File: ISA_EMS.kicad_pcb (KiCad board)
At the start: 2 copper layers, 176.5 x 102.9 mm, 57 parts, among them J1 ISA BUS, J2 EMS Address, J3 ROM Config, U1 74HCT688, U10 74HCT32, U11 74HCT04, U12 74ACT245, U13 AS6C4008-55PCN, U14 AS6C4008-55PCN, U15 AS6C4008-55PCN, U16 AS6C4008-55PCN, U17 74HCT138, U18 74LS573, U19 74LS573, U2 SST39SF040, U20 74LS573, U21 74LS573, U3 AS6C4008-55PCN, U4 AS6C4008-55PCN, U5 AS6C4008-55PCN, U6 AS6C4008-55PCN, U7 74HCT688, U8 74HCT688, U9 74HCT139

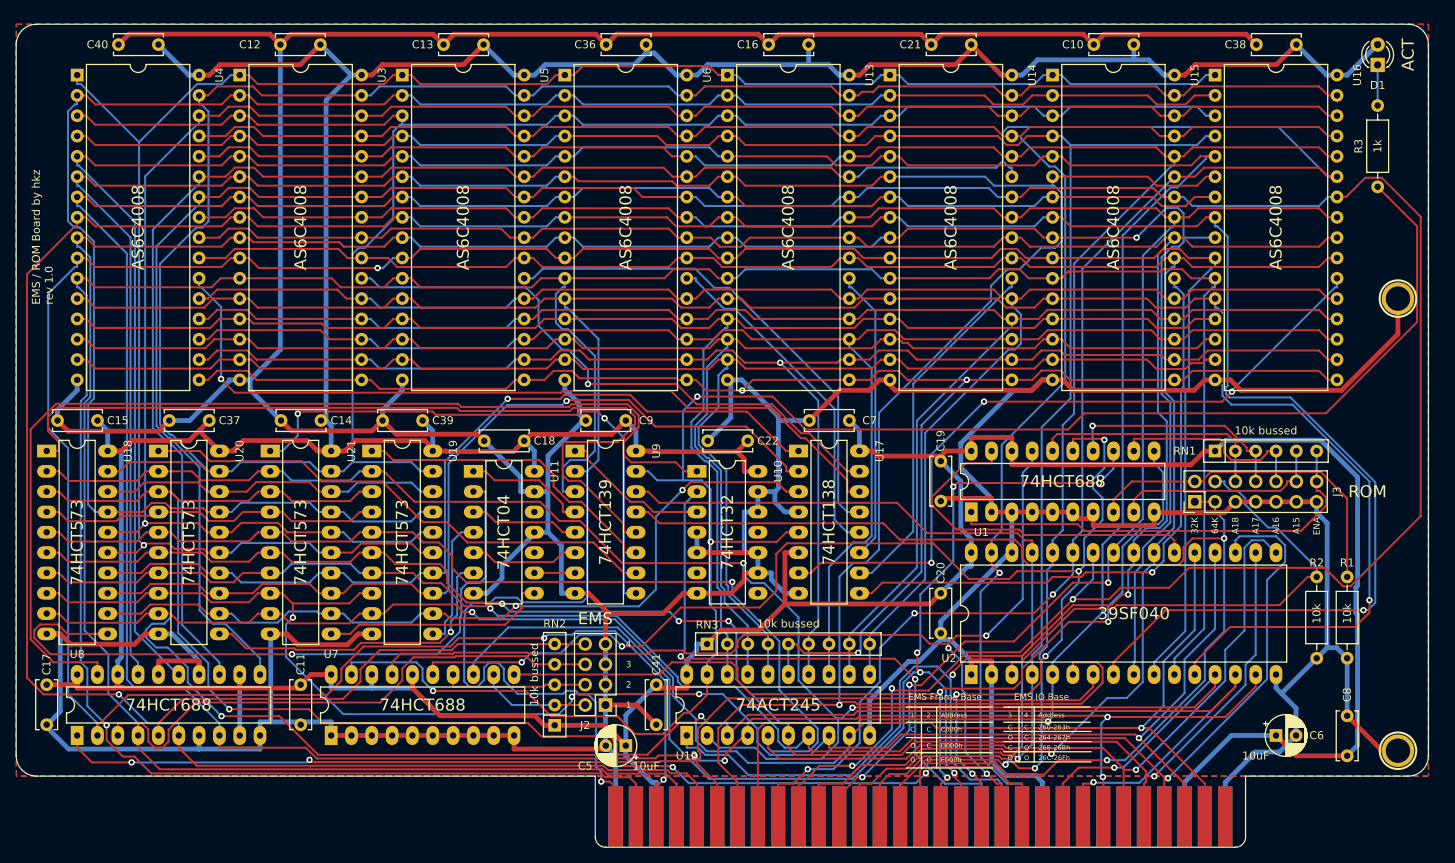
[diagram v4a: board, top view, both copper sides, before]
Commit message: Reorganize board a bit
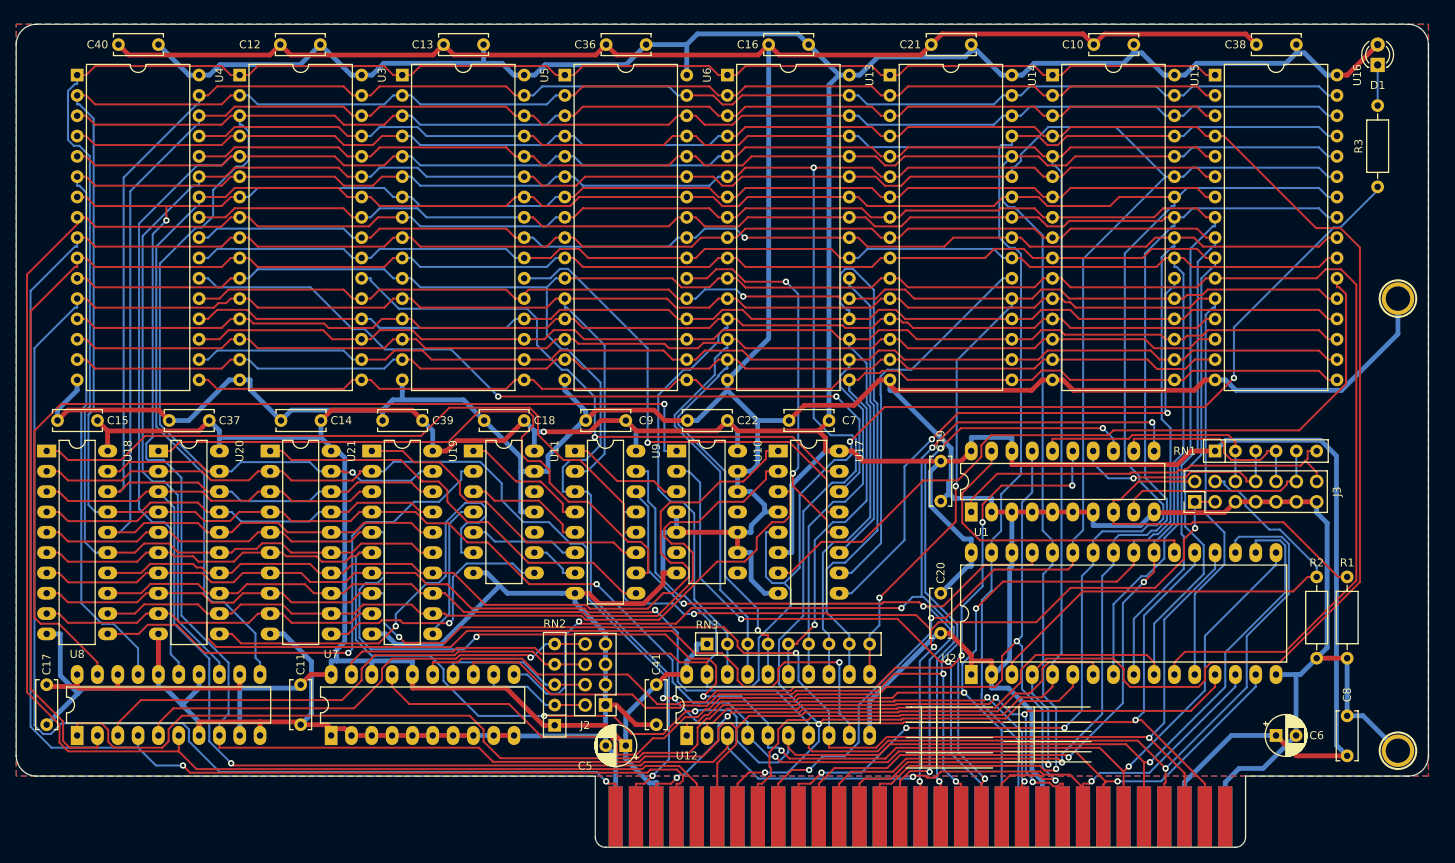
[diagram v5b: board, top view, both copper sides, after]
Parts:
- moved U10 3.59 mm to (221.0, 153.7)
- moved C22 3.59 mm to (227.3, 149.9)
- moved U11 2.54 mm to (195.6, 153.7)
- moved C18 2.54 mm to (201.9, 149.9)
- moved C7 2.54 mm to (240.0, 149.9)
- moved U17 2.54 mm to (233.7, 153.7)
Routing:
- net /A12: track 254.1 -> 306.1 mm
- net /A1: track 367.2 -> 315.3 mm
- net /D2: track 229.2 -> 182.6 mm, vias 5 -> 3
- net /A9: track 375.9 -> 337.3 mm
- net /A4: track 402.8 -> 370.6 mm, vias 2 -> 0
- net /A18: track 162.4 -> 131.2 mm, vias 7 -> 4
- net /A15: track 153.0 -> 122.2 mm, vias 2 -> 4
- net /A0: track 334.6 -> 362.7 mm, vias 2 -> 1
- net /D0: track 220.8 -> 195.4 mm, vias 3 -> 5
- net /D7: track 194.3 -> 218.9 mm
- net GND: track 908.6 -> 884.8 mm
- net /A8: track 357.7 -> 334.0 mm, vias 3 -> 2
- net /~REG0-OE: track 108.7 -> 86.7 mm
- net /REG0-LOAD: track 87.4 -> 65.9 mm
- net /D4: track 199.3 -> 219.2 mm, vias 4 -> 3
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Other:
- board text removed: "1"
- board text removed: "10k"
- board text removed: "10k bussed"
- board text removed: "10uF"
- board text removed: "1k"
- board text removed: "2"
- board text removed: "260-263h"
- board text removed: "264-267h"
- board text removed: "268-26Bh"
- board text removed: "26C-26Fh"
- board text removed: "3"
- board text removed: "32K"
- board text removed: "39SF040"
- board text removed: "4"
- board text removed: "64K"
- board text removed: "74ACT245"
- board text removed: "74HCT04"
- board text removed: "74HCT138"
- board text removed: "74HCT139"
- board text removed: "74HCT32"
- board text removed: "74HCT573"
- board text removed: "74HCT688"
- board text removed: "A15"
- board text removed: "A16"
- board text removed: "A17"
- board text removed: "A18"
- board text removed: "ACT"
- board text removed: "AS6C4008"
- board text removed: "Address"
- board text removed: "C"
- board text removed: "C000h"
- board text removed: "D000h"
- board text removed: "E000h"
- board text removed: "EMS"
- board text removed: "EMS / ROM Board by hkz rev 1.0"
- board text removed: "EMS Frame Base"
- board text removed: "EMS IO Base"
- board text removed: "ENA"
- board text removed: "O"
- board text removed: "ROM"

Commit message: Redoing silkscreen
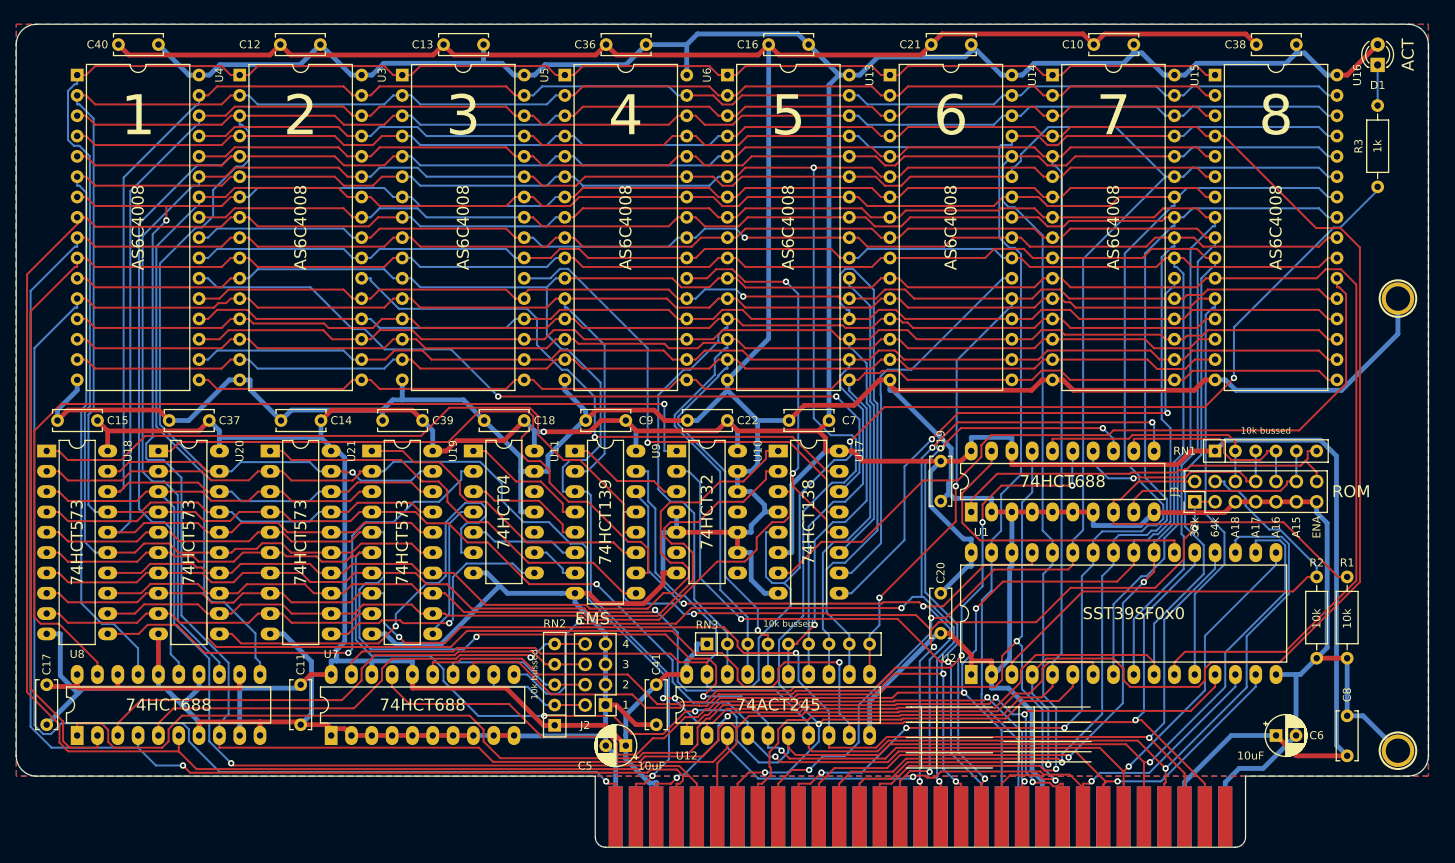
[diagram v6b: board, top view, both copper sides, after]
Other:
- board text added: "1"
- board text added: "10k"
- board text added: "10k bussed"
- board text added: "10uF"
- board text added: "1k"
- board text added: "2"
- board text added: "3"
- board text added: "32k"
- board text added: "4"
- board text added: "5"
- board text added: "6"
- board text added: "64k"
- board text added: "7"
- board text added: "74ACT245"
- board text added: "74HCT04"
- board text added: "74HCT138"
- board text added: "74HCT139"
- board text added: "74HCT32"
- board text added: "74HCT573"
- board text added: "74HCT688"
- board text added: "8"
- board text added: "A15"
- board text added: "A16"
- board text added: "A17"
- board text added: "A18"
- board text added: "ACT"
- board text added: "AS6C4008"
- board text added: "EMS"
- board text added: "ENA"
- board text added: "ROM"
- board text added: "SST39SF0x0"
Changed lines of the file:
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@@
   (general
     (thickness 1.6)
-    (drawings 41)
+    (drawings 92)
     (tracks 3500)
     (zones 0)
@@
   (page A3)
   (layers
-    (0 F.Cu signal)
-    (31 B.Cu signal)
+    (0 F.Cu signal hide)
+    (31 B.Cu signal hide)
     (32 B.Adhes user)
     (33 F.Adhes user)
@@
     (descr "Through hole straight pin header, 2x07, 2.54mm pitch, double rows")
     (tags "Through hole pin header THT 2x07 2.54mm double row")
-    (fp_text reference J3 (at 1.27 17.78 90) (layer F.SilkS)
+    (fp_text reference J3 (at 1.27 -2.54 90) (layer F.SilkS)
       (effects (font (size 1 1) (thickness 0.15)))
     )
@@
     )
   )
+  (gr_text A15 (at 298.45 163.195 90) (layer F.SilkS)
+    (effects (font (size 1 1) (thickness 0.25)))
+  )
+  (gr_text A16 (at 295.91 163.195 90) (layer F.SilkS)
+    (effects (font (size 1 1) (thickness 0.25)))
+  )
+  (gr_text A17 (at 293.37 163.195 90) (layer F.SilkS)
+    (effects (font (size 1 1) (thickness 0.25)))
+  )
+  (gr_text A18 (at 290.83 163.195 90) (layer F.SilkS)
+    (effects (font (size 1 1) (thickness 0.25)))
+  )
+  (gr_text ENA (at 300.99 163.195 90) (layer F.SilkS)
+    (effects (font (size 1 1) (thickness 0.25)))
+  )
+  (gr_text 64k (at 288.29 163.195 90) (layer F.SilkS)
+    (effects (font (size 1 1) (thickness 0.25)))
+  )
+  (gr_text 32k (at 285.75 163.195 90) (layer F.SilkS)
+    (effects (font (size 1 1) (thickness 0.25)))
+  )
+  (gr_text 4 (at 214.63 177.8) (layer F.SilkS)
+    (effects (font (size 1 1) (thickness 0.25)))
+  )
+  (gr_text 3 (at 214.63 180.34) (layer F.SilkS)
+    (effects (font (size 1 1) (thickness 0.25)))
+  )
+  (gr_text 2 (at 214.63 182.88) (layer F.SilkS)
+    (effects (font (size 1 1) (thickness 0.25)))
+  )
+  (gr_text 1 (at 214.63 185.42) (layer F.SilkS)
+    (effects (font (size 1 1) (thickness 0.25)))
+  )
+  (gr_text EMS (at 208.28 174.625) (layer F.SilkS)
+    (effects (font (size 1.5 1.5) (thickness 0.3)) (justify left))
+  )
+  (gr_text ROM (at 302.895 158.75) (layer F.SilkS)
+    (effects (font (size 1.5 1.5) (thickness 0.3)) (justify left))
+  )
+  (gr_text "10k bussed" (at 203.2 181.61 90) (layer F.SilkS)
+    (effects (font (size 0.8 0.8) (thickness 0.2)))
+  )
+  (gr_text "10k bussed" (at 234.95 175.26) (layer F.SilkS)
+    (effects (font (size 0.8 0.8) (thickness 0.2)))
+  )
+  (gr_text "10k bussed" (at 294.64 151.13) (layer F.SilkS)
+    (effects (font (size 0.8 0.8) (thickness 0.2)))
+  )
+  (gr_text 10uF (at 217.805 193.04) (layer F.SilkS)
+    (effects (font (size 1 1) (thickness 0.25)))
+  )
+  (gr_text 10uF (at 292.735 191.77) (layer F.SilkS)
+    (effects (font (size 1 1) (thickness 0.25)))
+  )
+  (gr_text 10k (at 304.8 174.625 90) (layer F.SilkS)
+    (effects (font (size 1 1) (thickness 0.25)))
+  )
+  (gr_text 10k (at 300.99 174.625 90) (layer F.SilkS)
+    (effects (font (size 1 1) (thickness 0.25)))
+  )
+  (gr_text 1k (at 308.61 115.57 90) (layer F.SilkS)
+    (effects (font (size 1 1) (thickness 0.25)))
+  )
+  (gr_text ACT (at 312.42 104.14 90) (layer F.SilkS)
+    (effects (font (size 1.5 1.5) (thickness 0.3)))
+  )
+  (gr_text 8 (at 295.91 111.76) (layer F.SilkS)
+    (effects (font (size 5 5) (thickness 0.9)))
+  )
+  (gr_text 7 (at 275.59 111.76) (layer F.SilkS)
+    (effects (font (size 5 5) (thickness 0.9)))
+  )
+  (gr_text 6 (at 255.27 111.76) (layer F.SilkS)
+    (effects (font (size 5 5) (thickness 0.9)))
+  )
+  (gr_text 5 (at 234.95 111.76) (layer F.SilkS)
+    (effects (font (size 5 5) (thickness 0.9)))
+  )
+  (gr_text 4 (at 214.63 111.76) (layer F.SilkS)
+    (effects (font (size 5 5) (thickness 0.9)))
+  )
+  (gr_text 3 (at 194.31 111.76) (layer F.SilkS)
+    (effects (font (size 5 5) (thickness 0.9)))
+  )
+  (gr_text 2 (at 173.99 111.76) (layer F.SilkS)
+    (effects (font (size 5 5) (thickness 0.9)))
+  )
+  (gr_text 1 (at 153.67 111.76) (layer F.SilkS)
+    (effects (font (size 5 5) (thickness 0.9)))
+  )
+  (gr_text AS6C4008 (at 295.91 125.73 90) (layer F.SilkS)
+    (effects (font (size 1.5 1.5) (thickness 0.3)))
+  )
+  (gr_text AS6C4008 (at 275.59 125.73 90) (layer F.SilkS)
+    (effects (font (size 1.5 1.5) (thickness 0.3)))
+  )
+  (gr_text AS6C4008 (at 255.27 125.73 90) (layer F.SilkS)
+    (effects (font (size 1.5 1.5) (thickness 0.3)))
+  )
+  (gr_text AS6C4008 (at 234.95 125.73 90) (layer F.SilkS)
+    (effects (font (size 1.5 1.5) (thickness 0.3)))
+  )
+  (gr_text AS6C4008 (at 214.63 125.73 90) (layer F.SilkS)
+    (effects (font (size 1.5 1.5) (thickness 0.3)))
+  )
+  (gr_text AS6C4008 (at 194.31 125.73 90) (layer F.SilkS)
+    (effects (font (size 1.5 1.5) (thickness 0.3)))
+  )
+  (gr_text AS6C4008 (at 173.99 125.73 90) (layer F.SilkS)
+    (effects (font (size 1.5 1.5) (thickness 0.3)))
+  )
+  (gr_text AS6C4008 (at 153.67 125.73 90) (layer F.SilkS)
+    (effects (font (size 1.5 1.5) (thickness 0.3)))
+  )
+  (gr_text 74HCT138 (at 237.49 162.56 90) (layer F.SilkS)
+    (effects (font (size 1.5 1.5) (thickness 0.3)))
+  )
+  (gr_text 74HCT32 (at 224.79 161.29 90) (layer F.SilkS)
+    (effects (font (size 1.5 1.5) (thickness 0.3)))
+  )
+  (gr_text 74HCT139 (at 212.09 162.56 90) (layer F.SilkS)
+    (effects (font (size 1.5 1.5) (thickness 0.3)))
+  )
+  (gr_text 74HCT04 (at 199.39 161.29 90) (layer F.SilkS)
+    (effects (font (size 1.5 1.5) (thickness 0.3)))
+  )
+  (gr_text 74HCT573 (at 186.69 165.1 90) (layer F.SilkS)
+    (effects (font (size 1.5 1.5) (thickness 0.3)))
+  )
+  (gr_text 74HCT573 (at 173.99 165.1 90) (layer F.SilkS)
+    (effects (font (size 1.5 1.5) (thickness 0.3)))
+  )
+  (gr_text 74HCT573 (at 160.02 165.1 90) (layer F.SilkS)
+    (effects (font (size 1.5 1.5) (thickness 0.3)))
+  )
+  (gr_text 74HCT573 (at 146.05 165.1 90) (layer F.SilkS)
+    (effects (font (size 1.5 1.5) (thickness 0.3)))
+  )
+  (gr_text 74HCT688 (at 157.48 185.42) (layer F.SilkS)
+    (effects (font (size 1.5 1.5) (thickness 0.3)))
+  )
+  (gr_text 74HCT688 (at 269.24 157.48) (layer F.SilkS)
+    (effects (font (size 1.5 1.5) (thickness 0.3)))
+  )
+  (gr_text 74HCT688 (at 189.23 185.42) (layer F.SilkS)
+    (effects (font (size 1.5 1.5) (thickness 0.3)))
+  )
+  (gr_text 74ACT245 (at 233.68 185.42) (layer F.SilkS)
+    (effects (font (size 1.5 1.5) (thickness 0.3)))
+  )
+  (gr_text SST39SF0x0 (at 278.13 173.99) (layer F.SilkS)
+    (effects (font (size 1.5 1.5) (thickness 0.3)))
+  )
   (gr_line (start 261.874 192.532) (end 272.796 192.532) (layer F.SilkS) (width 0.12))
